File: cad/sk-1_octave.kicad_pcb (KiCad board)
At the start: 2 copper layers, 36 x 16 mm, 16 parts, among them U1 4069, U2 74HC74, U3 74LS157

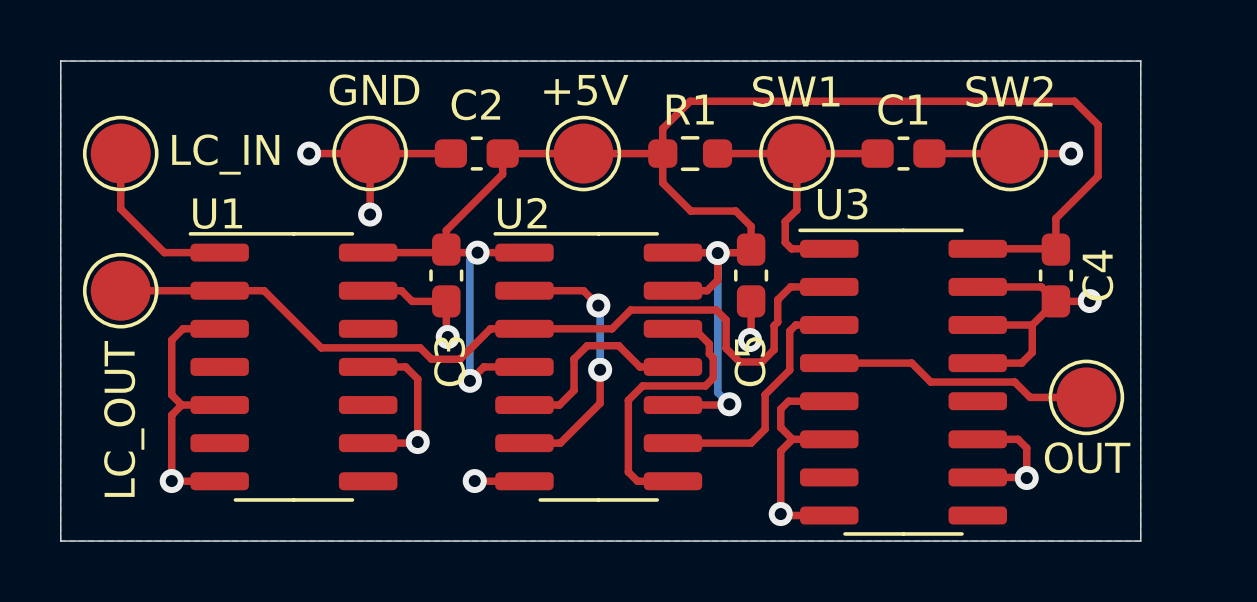
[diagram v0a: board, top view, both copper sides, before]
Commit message: Added output signal conditioning.
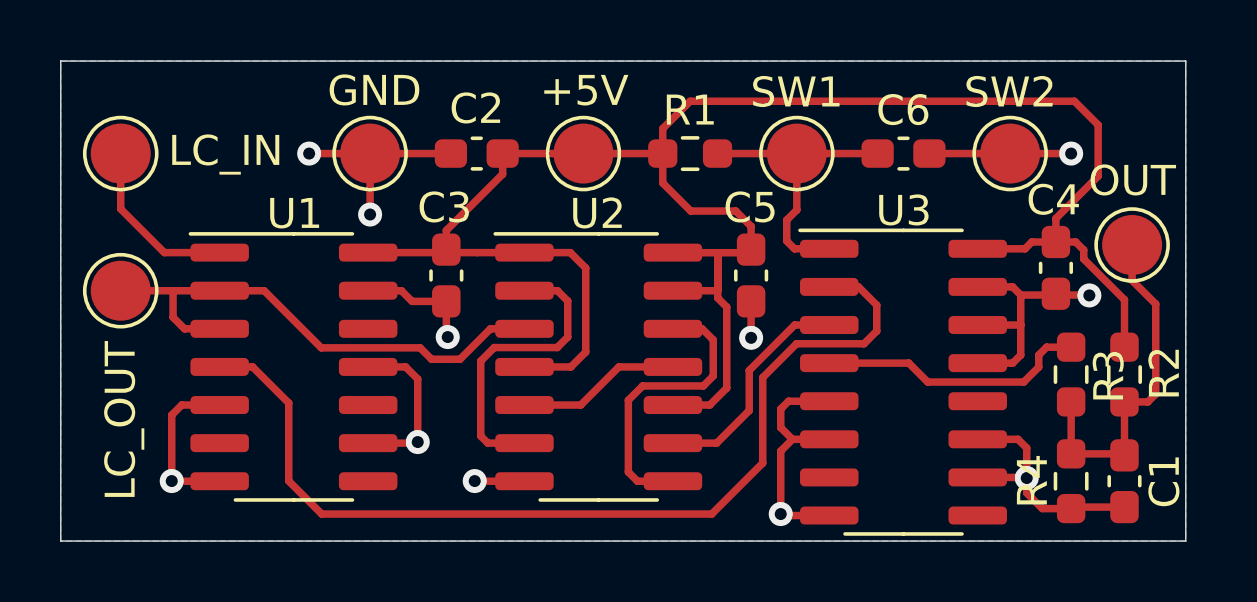
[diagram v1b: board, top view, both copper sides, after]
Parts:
- added C6: 100n, Capacitor_SMD:C_0603_1608Metric_Pad1.08x0.95mm_HandSolder, F.Cu at (101.1, 100.6)
- added R2: 4k7, Resistor_SMD:R_0603_1608Metric_Pad0.98x0.95mm_HandSolder, F.Cu at (108.5, 108.0)
- added R3: 1k, Resistor_SMD:R_0603_1608Metric_Pad0.98x0.95mm_HandSolder, F.Cu at (106.7, 108.0)
- added R4: 4k7, Resistor_SMD:R_0603_1608Metric_Pad0.98x0.95mm_HandSolder, F.Cu at (106.7, 111.5)
- C1: value 100n -> 18p
- R1: value R -> 4k7
- moved C1 13.2 mm to (108.5, 111.5), turned to 270 degrees
- moved TP1 5.30 mm to (108.7, 103.6)
- moved C4 0.25 mm to (106.2, 104.4)
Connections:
- R1 pad 2: Net-(C1-Pad1) -> Net-(C6-Pad1)
- TP1 pad 1: Net-(TP1-Pad1) -> Net-(C1-Pad1)
- TP4 pad 1: Net-(C1-Pad1) -> Net-(C6-Pad1)
- U1 pad 3: GND -> Net-(TP3-Pad1)
- U3 pad 1: Net-(C1-Pad1) -> Net-(C6-Pad1)
- U3 pad 2: Net-(TP3-Pad1) -> Net-(U1-Pad4)
- U3 pad 4: Net-(TP1-Pad1) -> Net-(R3-Pad2)
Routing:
- net Net-(U1-Pad4): track 0.00 -> 32.4 mm
- net Net-(TP3-Pad1): track 28.5 -> 17.4 mm
- net Net-(C6-Pad1): track 0.00 -> 9.92 mm
- net Net-(TP1-Pad1): track 9.04 -> 0.00 mm
- net Net-(R3-Pad2): track 0.00 -> 9.04 mm
- net +5V: track 62.0 -> 67.6 mm, vias 4 -> 0
- net Net-(C1-Pad1): track 10.0 -> 11.8 mm
- net Net-(U2-Pad11): track 6.68 -> 5.48 mm
- net Net-(U2-Pad2): track 9.02 -> 10.1 mm, vias 2 -> 0
- net GND: track 56.1 -> 55.2 mm
- net Net-(U2-Pad9): track 8.28 -> 7.62 mm
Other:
- board size 36 x 16 mm -> 37.5 x 16 mm

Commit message: Minor cleanup of PCB. Generated gerbers and drill files. Created BOM.
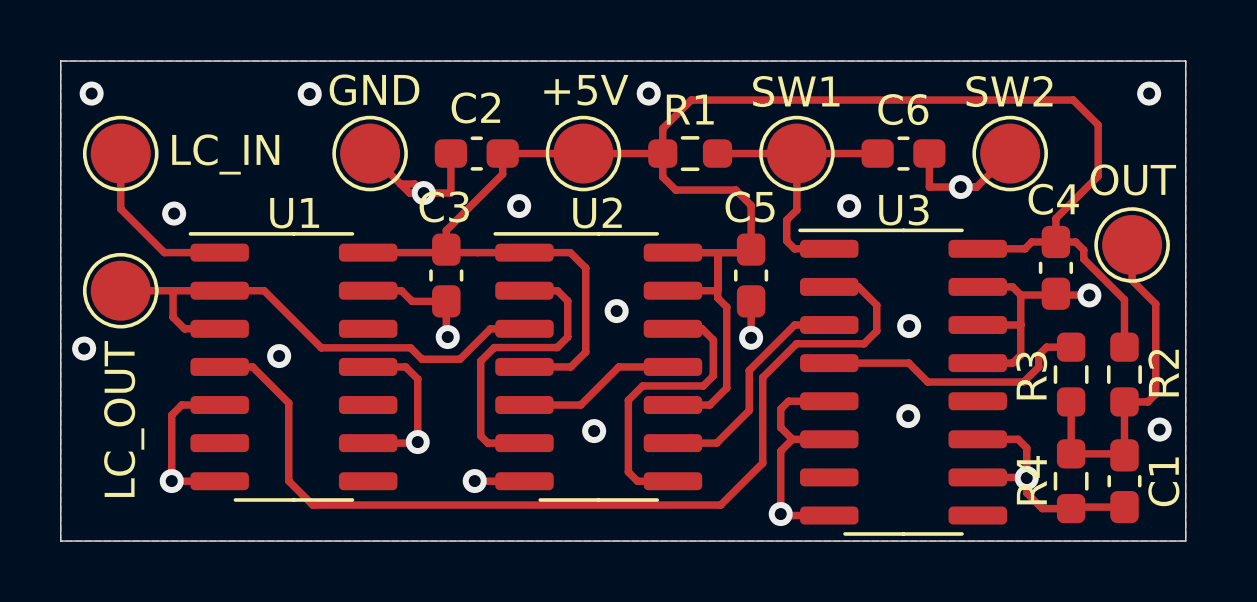
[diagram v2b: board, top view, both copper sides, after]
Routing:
- net GND: track 55.2 -> 54.0 mm, vias 11 -> 24
- added copper zone on F.Cu, net GND
